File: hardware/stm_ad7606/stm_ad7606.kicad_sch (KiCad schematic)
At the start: 28 parts, among them J1 Conn_01x02_Female, J2 USB_B_Micro, J4 AD7606 Interface, J5 SWD Conn, U1 STM32F103C8Tx, U2 AMS1117-3.3, Y1 8MHz

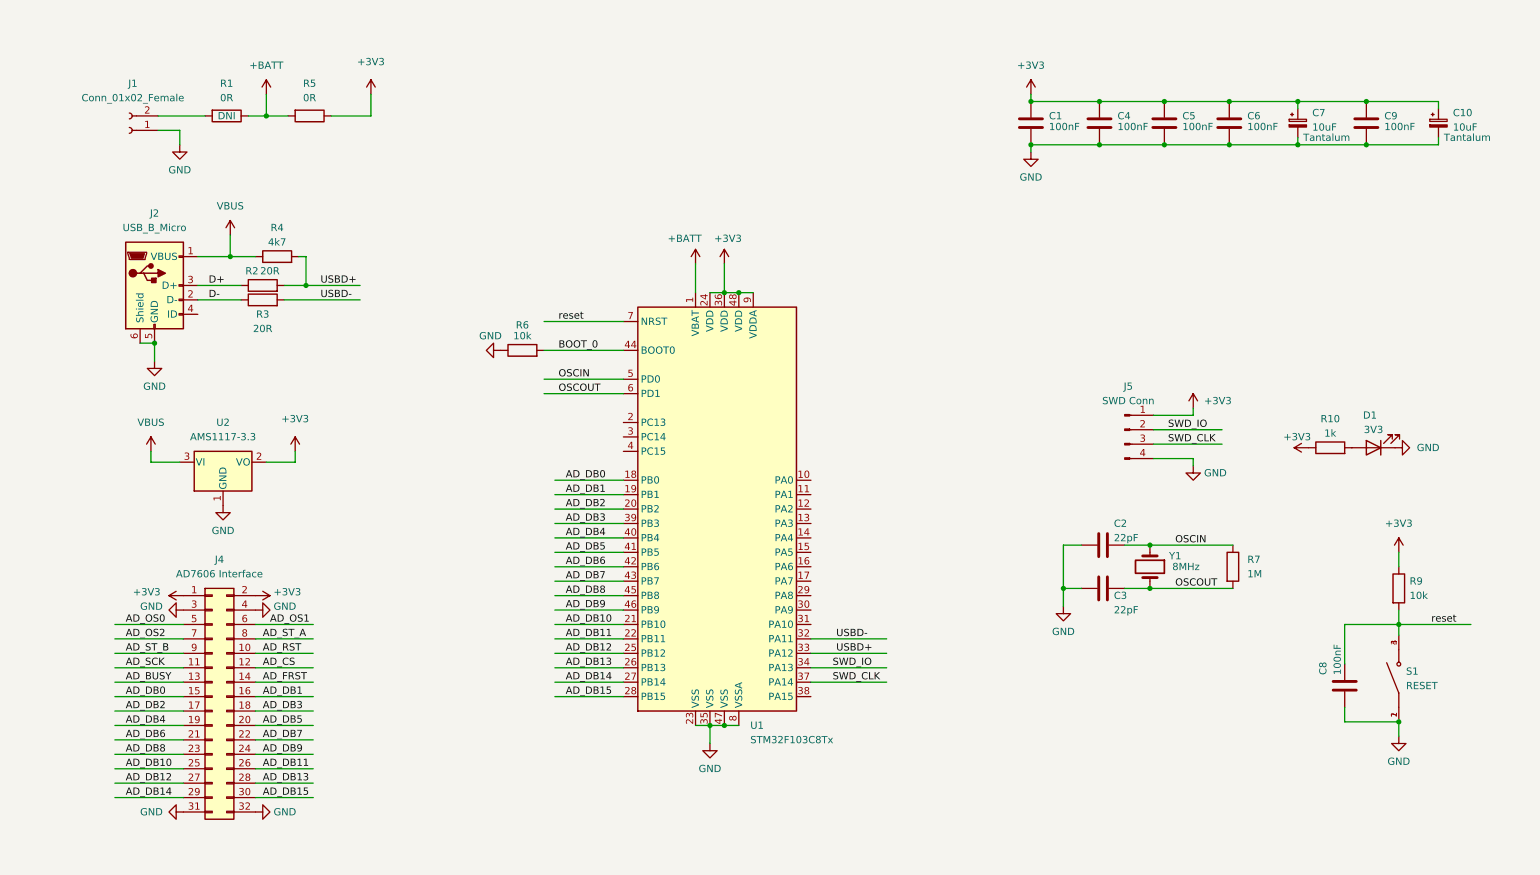
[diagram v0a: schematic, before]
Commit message: feat[hw]: add interface connection MCU vs 7606
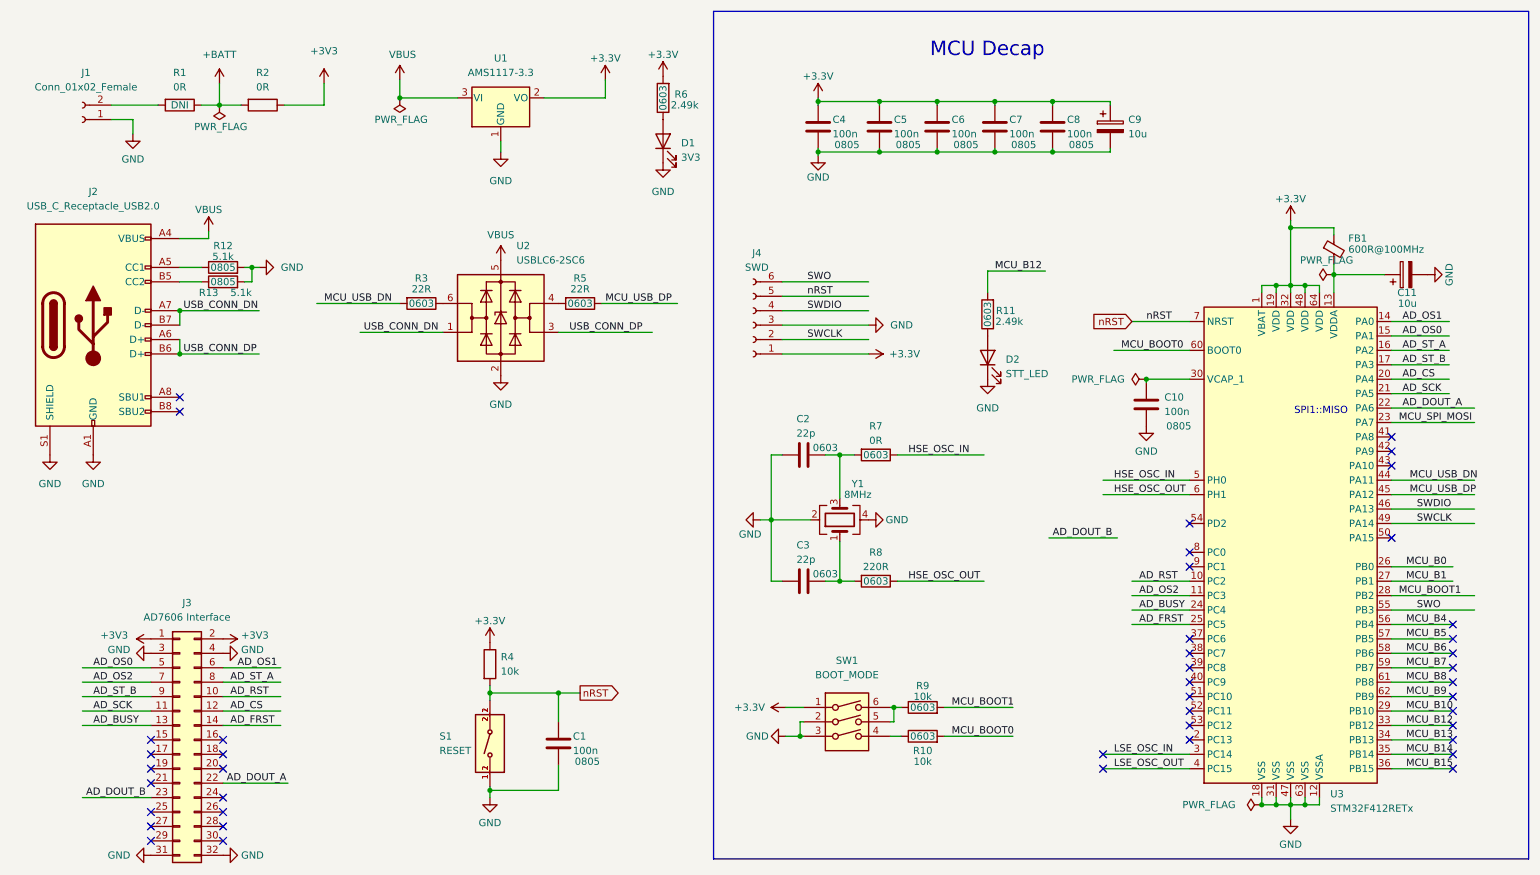
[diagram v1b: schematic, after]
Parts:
- removed C10, C7: 10uF, Capacitor_Tantalum_SMD:CP_EIA-3216-10_Kemet-I, symbol Device:C_Polarized_Small
- removed C9: 100nF, Capacitor_SMD:C_0805_2012Metric, symbol Device:C
- removed J2: USB_B_Micro, Connector_USB:USB_Micro-B_Molex-105017-0001, symbol Connector:USB_B_Micro
- removed J5: SWD Conn, Connector_PinHeader_2.54mm:PinHeader_1x04_P2.54mm_Vertical, symbol Connector:Conn_01x04_Male
- removed R2: 20R, Resistor_SMD:R_0805_2012Metric, symbol Device:R
- removed S1: RESET, SW1437565-9:SW_4-1437565-9, symbol SW1437565-9:4-1437565-9
- removed U1: STM32F103C8Tx, Package_QFP:LQFP-48_7x7mm_P0.5mm, symbol MCU_ST_STM32F1:STM32F103C8Tx
- removed U2: AMS1117-3.3, Package_TO_SOT_SMD:SOT-223-3_TabPin2, symbol Regulator_Linear:AMS1117-3.3
- removed Y1: 8MHz, Crystal:Crystal_SMD_HC49-SD, symbol Device:Crystal
- added C10, C7: 100n, Capacitor_SMD:C_0805_2012Metric, symbol Device:C
- added C11, C9: 10u, Capacitor_Tantalum_SMD:CP_EIA-3216-10_Kemet-I, symbol Device:C_Polarized
- added D2: STT_LED, LED_SMD:LED_0805_2012Metric, symbol Device:LED
- added FB1: 600R@100MHz, Inductor_SMD:L_0805_2012Metric, symbol Device:FerriteBead_Small
- added J2: USB_C_Receptacle_USB2.0, Connector_USB:USB_C_Receptacle_HRO_TYPE-C-31-M-12, symbol Connector:USB_C_Receptacle_USB2.0
- added J4: SWD, Connector_PinHeader_2.54mm:PinHeader_1x06_P2.54mm_Vertical, symbol Connector:Conn_01x06_Female
- added R11: 2.49k, Resistor_SMD:R_0603_1608Metric, symbol Device:R
- added R12, R13: 5.1k, Resistor_SMD:R_0805_2012Metric, symbol Device:R
- added R5: 22R, Resistor_SMD:R_0603_1608Metric, symbol Device:R
- added R8: 220R, Resistor_SMD:R_0603_1608Metric, symbol Device:R
- added S1: RESET, SW-KMR621NGLFS:SW_KMR621NGLFS, symbol KMR621NGLFS:KMR621NGLFS
- added SW1: BOOT_MODE, Button_Switch_SMD:SW_DIP_SPSTx03_Slide_KingTek_DSHP03TS_W7.62mm_P1.27mm, symbol Switch:SW_DIP_x03
- added U1: AMS1117-3.3, Package_TO_SOT_SMD:SOT-223-3_TabPin2, symbol Regulator_Linear:AMS1117-3.3
- added U2: USBLC6-2SC6, Package_TO_SOT_SMD:SOT-23-6, symbol Power_Protection:USBLC6-2SC6
- added U3: STM32F412RETx, Package_QFP:LQFP-64_10x10mm_P0.5mm, symbol MCU_ST_STM32F4:STM32F412RETx
- added Y1: 8MHz, Crystal:Crystal_SMD_5032-4Pin_5.0x3.2mm, symbol Device:Crystal_GND24
- C1, C4, C5, C6, C8: value 100nF -> 100n; Size (none) -> 0805
- C2, C3: value 22pF -> 22p; footprint Capacitor_SMD:C_0805_2012Metric -> Capacitor_SMD:C_0603_1608Metric; Size (none) -> 0603
- R10: value 1k -> 10k; footprint Resistor_SMD:R_0805_2012Metric -> Resistor_SMD:R_0603_1608Metric; Size (none) -> 0603
- R3: value 20R -> 22R; footprint Resistor_SMD:R_0805_2012Metric -> Resistor_SMD:R_0603_1608Metric; Size (none) -> 0603
- R4: value 4k7 -> 10k
- R6: value 10k -> 2.49k; footprint Resistor_SMD:R_0805_2012Metric -> Resistor_SMD:R_0603_1608Metric; Size (none) -> 0603
- R7: value 1M -> 0R; footprint Resistor_SMD:R_0805_2012Metric -> Resistor_SMD:R_0603_1608Metric; Size (none) -> 0603
- R9: footprint Resistor_SMD:R_0805_2012Metric -> Resistor_SMD:R_0603_1608Metric; Size (none) -> 0603
- renumbered J4 to J3, R5 to R2
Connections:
- net BOOT_0 is gone; now on net +3V3: R6.2
- net +3V3: now also C8.1, R4.1, C7.1, C9.1, FB1.1, J4.1 (Pin_1), SW1.1, U1.2 (VO), U3.1 (VBAT), U3.19 (VDD), U3.32 (VDD), U3.48 (VDD), U3.64 (VDD); no longer C1.1, R10.1, R9.1
- net AD_BUSY: now also U3.24 (PC4)
- net AD_CS: now also U3.20 (PA4)
- net AD_FRST: now also U3.25 (PC5)
- net AD_OS0: now also U3.15 (PA1)
- net AD_OS1: now also U3.14 (PA0)
- net AD_OS2: now also U3.11 (PC3)
- net AD_RST: now also U3.10 (PC2)
- net AD_SCK: now also U3.21 (PA5)
- net AD_ST_A: now also U3.16 (PA2)
- net AD_ST_B: now also U3.17 (PA3)
- net GND: now also C10.2, C11.2, C7.2, C9.2, D2.1 (K), J2.A1 (GND), J2.A12 (GND), J2.B1 (GND), J2.B12 (GND), J2.S1 (SHIELD), J4.3 (Pin_3), R12.2, R13.2, S1.1_1, S1.1_2, SW1.2, SW1.3, U1.1 (GND), U2.2 (GND), U3.12 (VSSA), U3.18 (VSS), U3.31 (VSS), U3.47 (VSS), U3.63 (VSS), Y1.2, Y1.4; no longer R6.1
- net VBUS: now also J2.A4 (VBUS), J2.A9 (VBUS), J2.B4 (VBUS), J2.B9 (VBUS), U1.3 (VI), U2.5 (VBUS); no longer R4.1
- net at D1.2 (A): now also R6.1; no longer R10.2
- net AD_DB0: no longer names the net of J3.15 (Pin_15)
- net AD_DB1: no longer names the net of J3.16 (Pin_16)
- net AD_DB10: no longer names the net of J3.25 (Pin_25)
- net AD_DB11: no longer names the net of J3.26 (Pin_26)
- net AD_DB12: no longer names the net of J3.27 (Pin_27)
- net AD_DB13: no longer names the net of J3.28 (Pin_28)
- net AD_DB14: no longer names the net of J3.29 (Pin_29)
- net AD_DB15: no longer names the net of J3.30 (Pin_30)
- net AD_DB2: no longer names the net of J3.17 (Pin_17)
- net AD_DB3: no longer names the net of J3.18 (Pin_18)
- net AD_DB4: no longer names the net of J3.19 (Pin_19)
- net AD_DB5: no longer names the net of J3.20 (Pin_20)
- net AD_DB6: no longer names the net of J3.21 (Pin_21)
- net AD_DB7 renamed AD_DOUT_A
- net AD_DOUT_A: now also U3.22 (PA6)
- net AD_DB8 renamed AD_DOUT_B
- net AD_DB9: no longer names the net of J3.24 (Pin_24)
- net D-: no longer names the net of R3.1
- net D-: now also U2.6 (I/O1)
- net OSCIN: no longer names the net of C2.1
- net OSCIN: now also R7.2, Y1.3; no longer R7.1
- net OSCOUT: no longer names the net of C3.1
- net OSCOUT: now also R8.2, Y1.1; no longer R7.2
- net USBD+ renamed nRST
- net nRST: now also C1.1, J4.5 (Pin_5), S1.2_1, S1.2_2, U3.7 (NRST)
- net USBD- renamed MCU_USB_DN
- net MCU_USB_DN: now also U3.44 (PA11)
- net reset renamed MCU_BOOT1
- net MCU_BOOT1: now also U3.28 (PB2); no longer C8.1
- new net: C11.1, FB1.2, U3.13 (VDDA)
- new net: C10.1, U3.30 (VCAP_1)
- new net: R5.2, U2.4 (I/O2)
- new net: J2.A5 (CC1), R12.1
- new net: J2.B5 (CC2), R13.1
- new net: R10.1, SW1.4
- new net: D2.2 (A), R11.1
- new net: R9.1, SW1.5, SW1.6
- new net HSE_OSC_IN: R7.1, U3.5 (PH0)
- new net HSE_OSC_OUT: R8.1, U3.6 (PH1)
- new net LSE_OSC_IN: U3.3 (PC14)
- new net LSE_OSC_OUT: U3.4 (PC15)
- new net MCU_B0: U3.26 (PB0)
- new net MCU_B1: U3.27 (PB1)
- new net MCU_B10: U3.29 (PB10)
- new net MCU_B12: R11.2, U3.33 (PB12)
- new net MCU_B13: U3.34 (PB13)
- new net MCU_B14: U3.35 (PB14)
- new net MCU_B15: U3.36 (PB15)
- new net MCU_B4: U3.56 (PB4)
- new net MCU_B5: U3.57 (PB5)
- new net MCU_B6: U3.58 (PB6)
- new net MCU_B7: U3.59 (PB7)
- new net MCU_B8: U3.61 (PB8)
- new net MCU_B9: U3.62 (PB9)
- new net MCU_BOOT0: R10.2, U3.60 (BOOT0)
- new net MCU_SPI_MOSI: U3.23 (PA7)
- new net MCU_USB_DP: R5.1, U3.45 (PA12)
- new net SWCLK: J4.2 (Pin_2), U3.49 (PA14)
- new net SWDIO: J4.4 (Pin_4), U3.46 (PA13)
- new net SWO: J4.6 (Pin_6), U3.55 (PB3)
- new net USB_CONN_DN: J2.A7 (D-), J2.B7 (D-), U2.1 (I/O1)
- new net USB_CONN_DP: J2.A6 (D+), J2.B6 (D+), U2.3 (I/O2)
- no-connect marks 0 -> 44
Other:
- note added: "MCU Decap"
- note added: "SPI1::MISO"
- moved on the sheet: J1, J3, R1, R2
